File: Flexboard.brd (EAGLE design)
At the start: 488.2 x 145.3 mm, 449 parts, among them J1 USB4105-GF-A, SW1 1825910-7, U1 MK22FX512AVLQ12, Y1 ABM3B-8.000MHZ-B2-T, Y2 ABS07-32.768KHZ-T

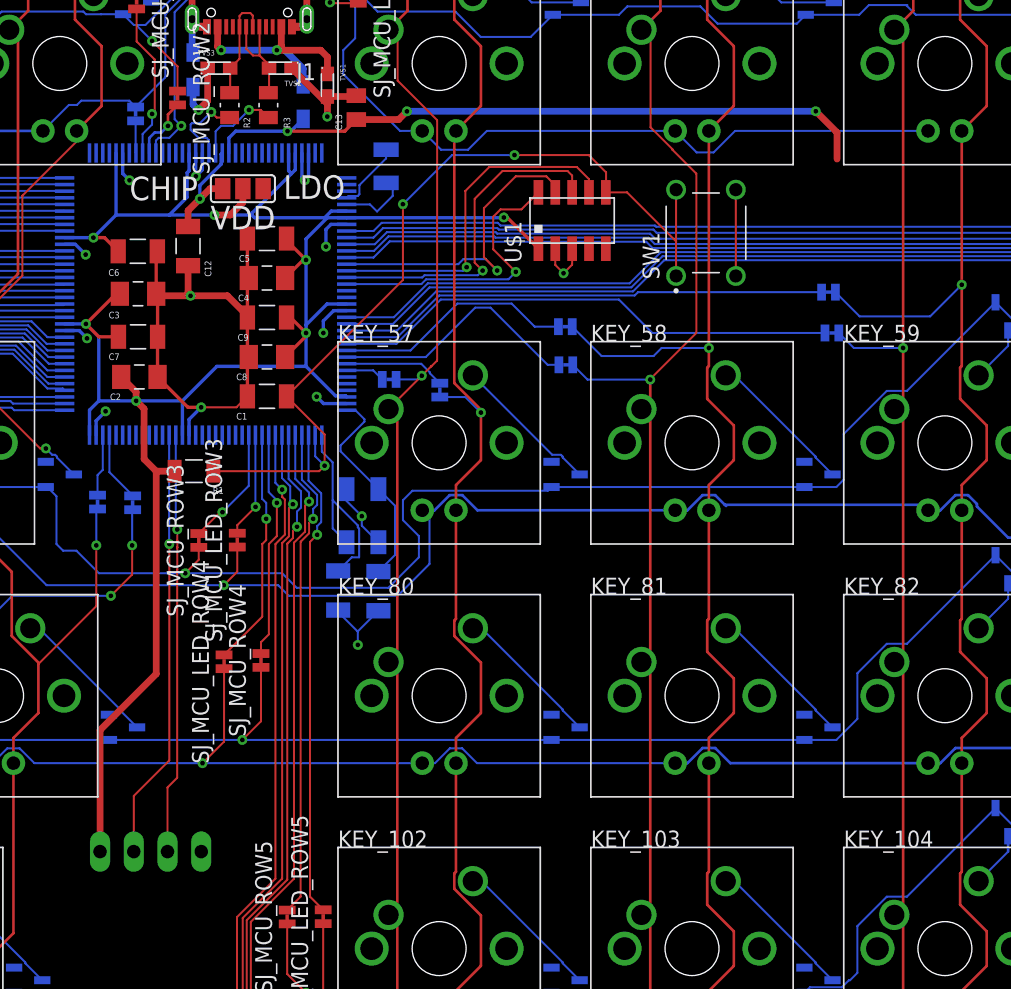
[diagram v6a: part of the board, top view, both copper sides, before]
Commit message: added LDO to design
LDO added, now just need power decoupling caps and diodes
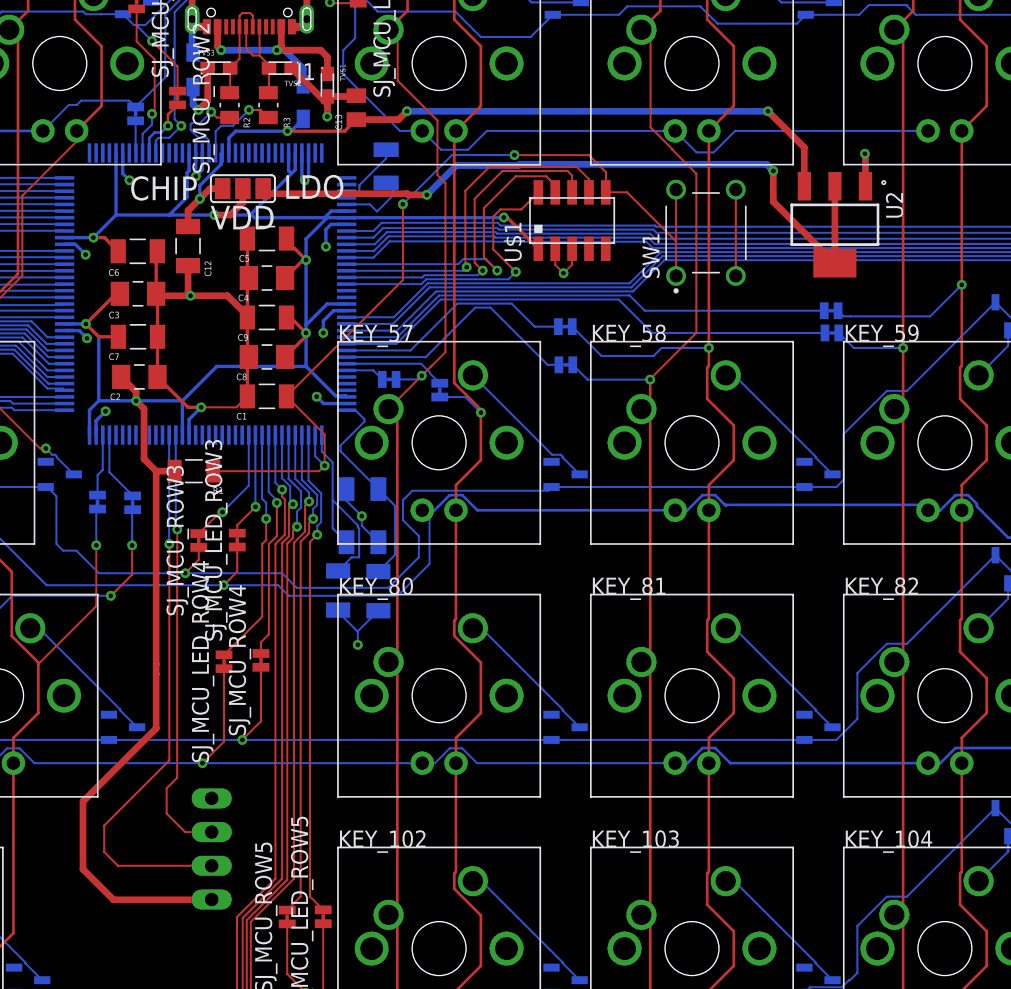
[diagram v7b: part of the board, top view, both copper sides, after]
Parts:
- added U2: NCP1117ST33T3G, NCP1117ST33T3G:SOT230P700X180-4N
- moved SV1 4.60 mm to (335.3, 55.1), turned to 90 degrees
- moved SJ_MCU_LED_COL20 1.41 mm to (382.0, 95.7)
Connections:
- net GND: now also U2.1
- net VLDO_33: now also U2.2, U2.4
- net VSYS_5V5: now also U2.3
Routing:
- net VLDO_33: track 0.00 -> 54.5 mm, vias 0 -> 2
- net VDD_3V3: track 168.1 -> 180.7 mm
- net UART0_TX: track 32.5 -> 42.0 mm
- net GND: track 101.8 -> 104.3 mm, vias 16 -> 17
- net UART0_RX: track 31.7 -> 32.9 mm
- net VSYS_5V5: track 52.0 -> 50.9 mm
- net LED_COL_20: track 139.8 -> 139.0 mm
- net LED_COL_20{MCU}: track 37.2 -> 37.8 mm
- net COL_18: track 118.4 -> 118.9 mm

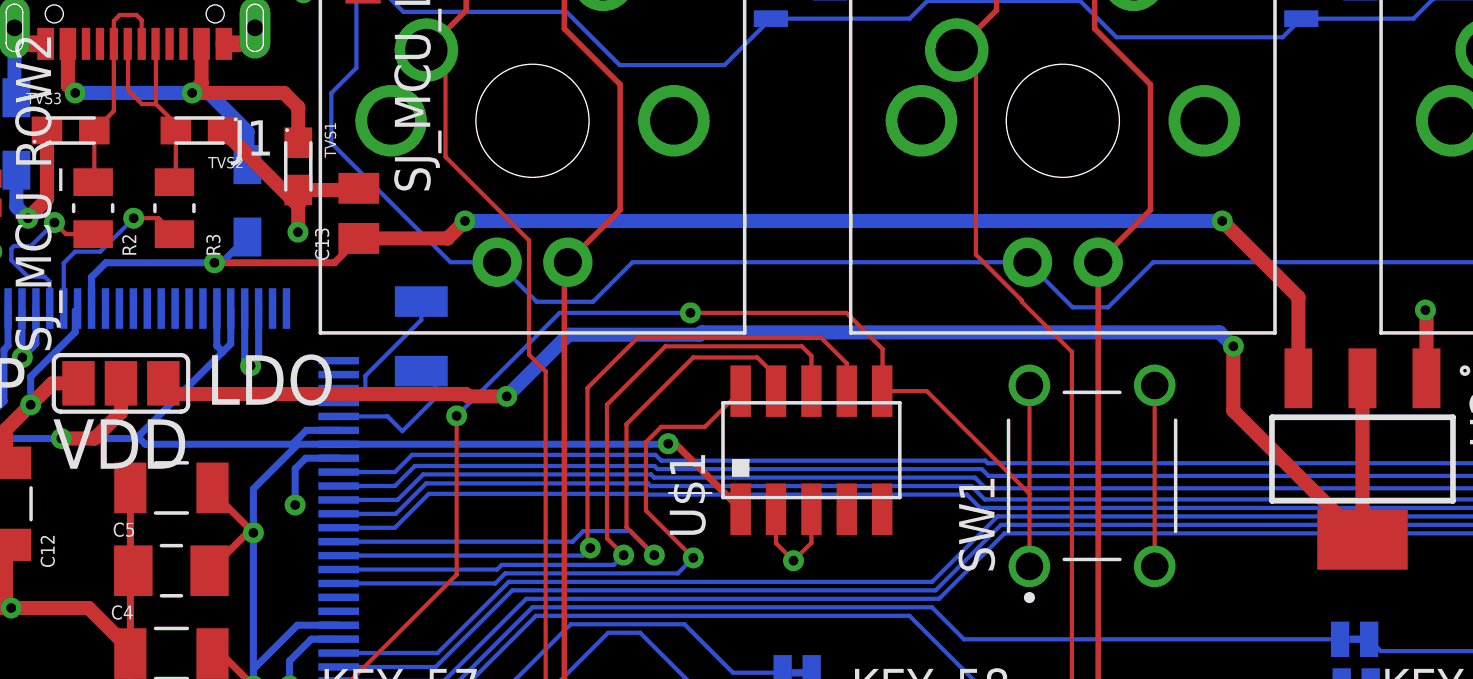
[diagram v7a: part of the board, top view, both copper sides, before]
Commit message: added all power domain components
Added schottky diode on 5V LDO power rail to protect LDO. Power domain
routing should be complete.
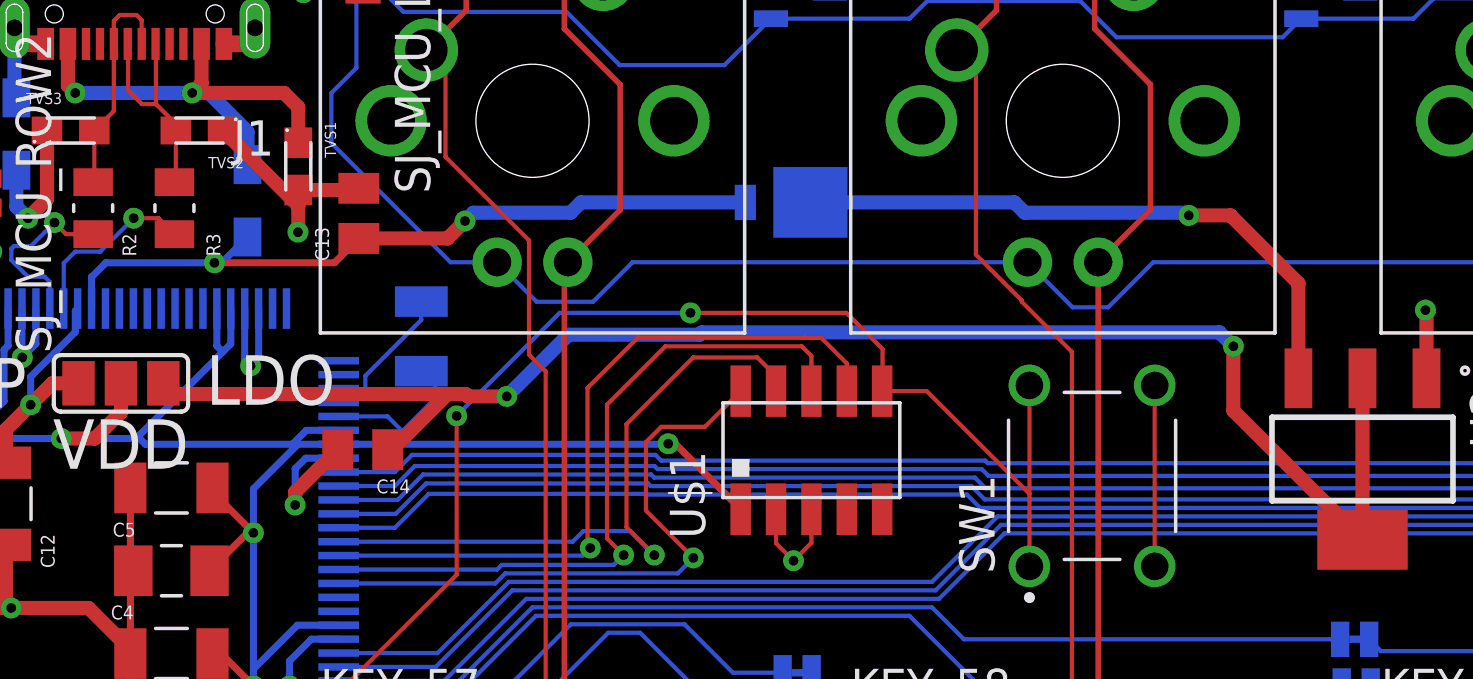
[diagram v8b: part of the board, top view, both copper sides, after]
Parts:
- added C14: 10uF, GRM21BC8YA106ME11L:CAPC2012X145N
- added D146: UPS115UE3/TR7, UPS115UE3-TR7:UPS115UE3/TR7
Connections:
- new net VLDO_5V5: D146.1, U2.3
- net GND: now also C14.2
- net VLDO_33: now also C14.1
- net VSYS_5V5: now also D146.2; no longer U2.3
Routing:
- net VSYS_5V5: track 50.9 -> 27.3 mm, vias 3 -> 2
- net VLDO_5V5: track 0.00 -> 22.1 mm, vias 0 -> 1
- net VLDO_33: track 54.5 -> 57.4 mm
- net GND: track 104.3 -> 106.9 mm
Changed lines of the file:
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@@
 <attribute name="PURCHASE-URL" value="https://pricing.snapeda.com/search/part/NCP1117ST33T3G/?ref=eda" x="382.2375" y="102.15" size="1.778" layer="27" rot="R270" display="off"/>
 </element>
+<element name="D146" library="UPS115UE3-TR7" package="UPS115UE3/TR7" value="UPS115UE3/TR7" x="360.75625" y="111.36875" smashed="yes" rot="MR0">
+<attribute name="NAME" x="364.56625" y="112.89275" size="1.27" layer="26" rot="MR0"/>
+</element>
+<element name="C14" library="GRM21BC8YA106ME11L" package="CAPC2012X145N" value="10uF" x="346.325" y="102.4875" smashed="yes" rot="R180">
+<attribute name="DESCRIPTION" value=" 0805 10 uF 35 V ±20% Tolerance X6S Multilayer Ceramic Capacitor " x="346.325" y="102.4875" size="1.778" layer="27" rot="R180" display="off"/>
+<attribute name="DIGI-KEY_PART_NUMBER" value="490-10505-2-ND" x="346.325" y="102.4875" size="1.778" layer="27" rot="R180" display="off"/>
+<attribute name="MF" value="Murata" x="346.325" y="102.4875" size="1.778" layer="27" rot="R180" display="off"/>
+<attribute name="MP" value="GRM21BC8YA106ME11L" x="346.325" y="102.4875" size="1.778" layer="27" rot="R180" display="off"/>
+<attribute name="NAME" x="348.035" y="101.4175" size="0.5" layer="25" rot="R180"/>
+<attribute name="PACKAGE" value="2012 Murata" x="346.325" y="102.4875" size="1.778" layer="27" rot="R180" display="off"/>
+<attribute name="PURCHASE-URL" value="https://pricing.snapeda.com/search/part/GRM21BC8YA106ME11L/?ref=eda" x="346.325" y="102.4875" size="1.778" layer="27" rot="R180" display="off"/>
+<attribute name="VALUE" x="348.035" y="103.5575" size="0.5" layer="27" rot="R180" align="top-left"/>
+</element>
 </elements>
 <signals>
@@
 <wire x1="384.5375" y1="107.4625" x2="384.5" y2="107.5" width="0.508" layer="1"/>
 <via x="384.5" y="107.5" extent="1-16" drill="0.35"/>
+<contactref element="C14" pad="2"/>
+<wire x1="345.425" y1="102.4875" x2="343.9" y2="100.9625" width="0.508" layer="1"/>
+<wire x1="343.9" y1="100.9625" x2="343.9" y2="100.5" width="0.508" layer="1"/>
 <wire x1="374.775" y1="104.79375" x2="384.5375" y2="105.05" width="0" layer="19" extent="1-1"/>
 <wire x1="362.44375" y1="100.34785" x2="374.775" y2="98.29375" width="0" layer="19" extent="1-1"/>
 <wire x1="345.462496875" y1="102.18125" x2="361.17375" y2="100.34785" width="0" layer="19" extent="1-16"/>
-<wire x1="342.3" y1="105.5" x2="345.462496875" y2="102.18125" width="0" layer="19" extent="16-16"/>
+<wire x1="342.3" y1="105.5" x2="345.425" y2="102.4875" width="0" layer="19" extent="1-1"/>
 <wire x1="344" y1="110.3" x2="342.5875" y2="107.556246875" width="0" layer="19" extent="16-16"/>
 <wire x1="341.3375" y1="117.06375" x2="341.3125" y2="113.95" width="0" layer="19" extent="1-1"/>
@@
 <wire x1="350.10959375" y1="104.4" x2="350.02499375" y2="104.4846" width="0.508" layer="1"/>
 <wire x1="339.5519" y1="104.4846" x2="339.16775" y2="104.86875" width="0.508" layer="1"/>
-<wire x1="350.02499375" y1="104.4846" x2="339.5519" y2="104.4846" width="0.508" layer="1"/>
+<wire x1="339.5519" y1="104.4846" x2="349.37500625" y2="104.4846" width="0.508" layer="1"/>
 <wire x1="377.1" y1="106.7" x2="358.50959375" y2="106.7" width="0.508" layer="16"/>
+<contactref element="C14" pad="1"/>
+<wire x1="350.02499375" y1="104.4846" x2="349.37500625" y2="104.4846" width="0.508" layer="1"/>
+<wire x1="347.37790625" y1="102.4875" x2="347.225" y2="102.4875" width="0.508" layer="1"/>
+<wire x1="349.37500625" y1="104.4846" x2="347.37790625" y2="102.4875" width="0.508" layer="1"/>
 </signal>
 <signal name="VSYS_5V5">
@@
 <wire x1="349.375" y1="110.075" x2="350" y2="110.7" width="0.508" layer="1"/>
 <via x="350" y="110.7" extent="1-16" drill="0.35"/>
-<contactref element="U2" pad="3"/>
-<wire x1="350" y1="110.7" x2="377.2" y2="110.7" width="0.508" layer="16"/>
-<via x="377.2" y="110.7" extent="1-16" drill="0.35"/>
-<wire x1="377.2" y1="110.7" x2="379.9375" y2="107.9625" width="0.508" layer="1"/>
-<wire x1="379.9375" y1="107.9625" x2="379.9375" y2="105.05" width="0.508" layer="1"/>
+<contactref element="D146" pad="2"/>
+<wire x1="353.7927375" y1="110.998" x2="354.1634875" y2="111.36875" width="0.508" layer="16"/>
+<wire x1="354.1634875" y1="111.36875" x2="360.07045" y2="111.36875" width="0.508" layer="16"/>
+<wire x1="350" y1="110.7" x2="350.298" y2="110.998" width="0.508" layer="16"/>
+<wire x1="350.298" y1="110.998" x2="353.7927375" y2="110.998" width="0.508" layer="16"/>
 </signal>
 <signal name="N$1">
@@
 <wire x1="333.8175" y1="115.195" x2="333.8875" y2="115.125" width="0.508" layer="16"/>
 </signal>
+<signal name="VLDO_5V5">
+<contactref element="U2" pad="3"/>
+<contactref element="D146" pad="1"/>
+<via x="376" y="110.9" extent="1-16" drill="0.35"/>
+<wire x1="362.40725" y1="111.36875" x2="369.7365125" y2="111.36875" width="0.508" layer="16"/>
+<wire x1="369.7365125" y1="111.36875" x2="370.1072625" y2="110.998" width="0.508" layer="16"/>
+<wire x1="375.902" y1="110.998" x2="376" y2="110.9" width="0.508" layer="16"/>
+<wire x1="370.1072625" y1="110.998" x2="375.902" y2="110.998" width="0.508" layer="16"/>
+<wire x1="376" y1="110.9" x2="377.5" y2="110.9" width="0.508" layer="1"/>
+<wire x1="379.9375" y1="108.4625" x2="379.9375" y2="105.05" width="0.508" layer="1"/>
+<wire x1="377.5" y1="110.9" x2="379.9375" y2="108.4625" width="0.508" layer="1"/>
+</signal>
 </signals>
